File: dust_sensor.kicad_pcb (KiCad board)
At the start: 2 copper layers, 50 x 45 mm, 32 parts, among them P1 ADC, P10 PWR, P2 POWER, P3 LCD, P4 LCD_RST, P5 SERIAL, P6 DHT, P7 SENSOR, P8 GPIOS, P9 DEEP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

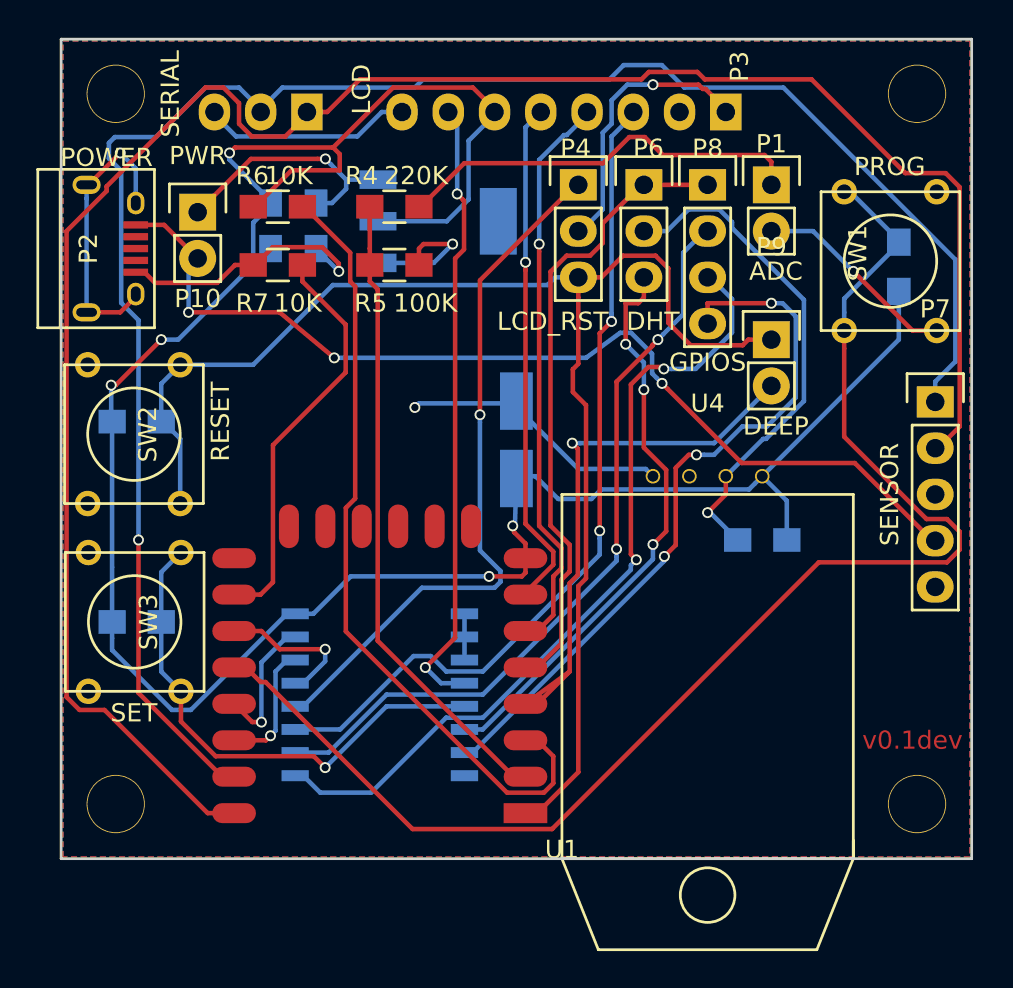
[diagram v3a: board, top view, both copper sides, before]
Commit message: PCB: remove LCD_RST jumper
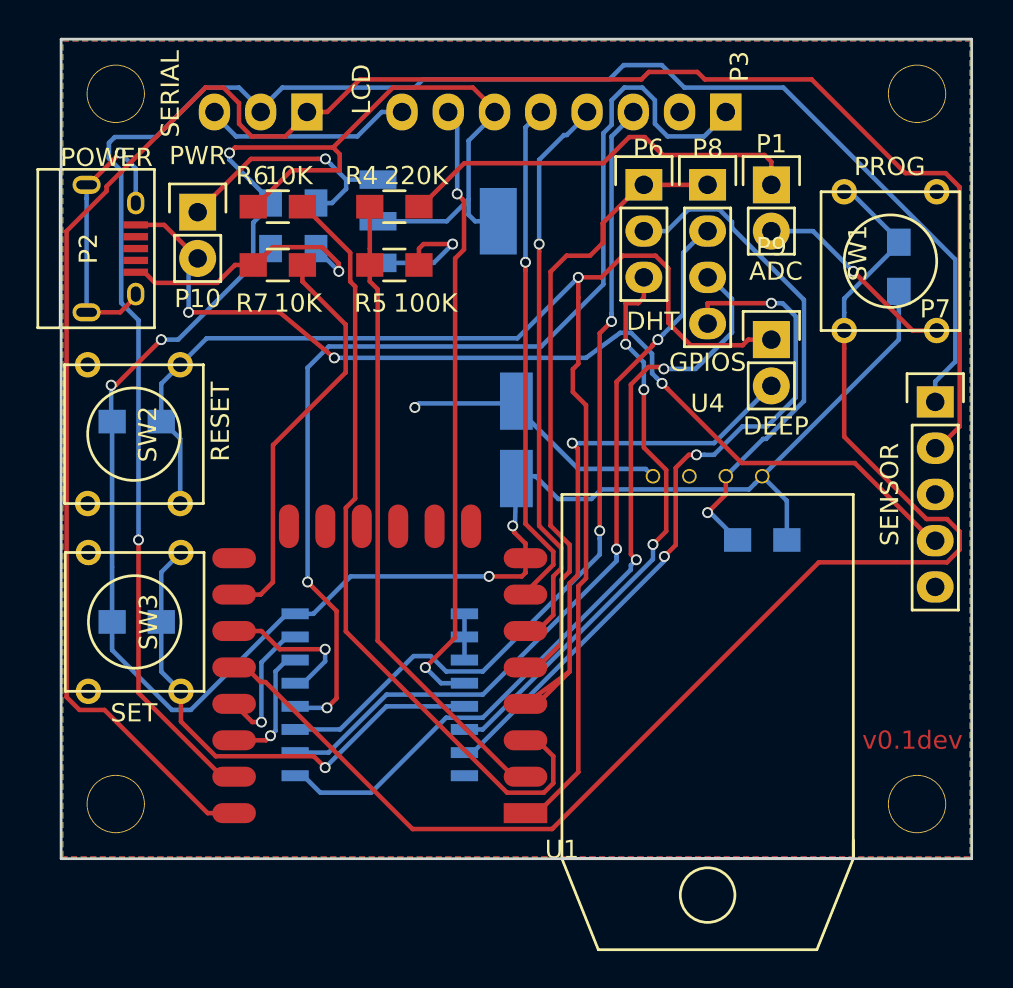
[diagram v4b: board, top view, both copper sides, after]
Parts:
- removed P4: LCD_RST, Pin_Headers:Pin_Header_Straight_1x03
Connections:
- P2 pad 2: Net-(P2-Pad2) -> (no net)
- P2 pad 3: Net-(P2-Pad3) -> (no net)
- P2 pad 4: Net-(P2-Pad4) -> (no net)
- P7 pad 5: Net-(P7-Pad5) -> (no net)
- U1 pad 10: Net-(U1-Pad10) -> (no net)
- U1 pad 11: Net-(U1-Pad11) -> (no net)
- U1 pad 12: Net-(U1-Pad12) -> (no net)
- U1 pad 13: Net-(U1-Pad13) -> (no net)
- U1 pad 14: Net-(U1-Pad14) -> (no net)
- U1 pad 9: Net-(U1-Pad9) -> (no net)
- U2 pad 4: (no net) -> +3V3
- U3 pad 12: Net-(P4-Pad1) -> Net-(P3-Pad1)
- U4 pad 3: Net-(U4-Pad3) -> (no net)
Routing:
- net Net-(P3-Pad1): track 15.5 -> 59.4 mm, vias 1 -> 2
- net Net-(P4-Pad1): track 38.7 -> 0.00 mm, vias 1 -> 0
- net +3V3: track 131.7 -> 134.4 mm
- net RESET: vias 0 -> 1

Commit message: PCB: SCH: choose ext_int/dht between GPIO2/GPIO14
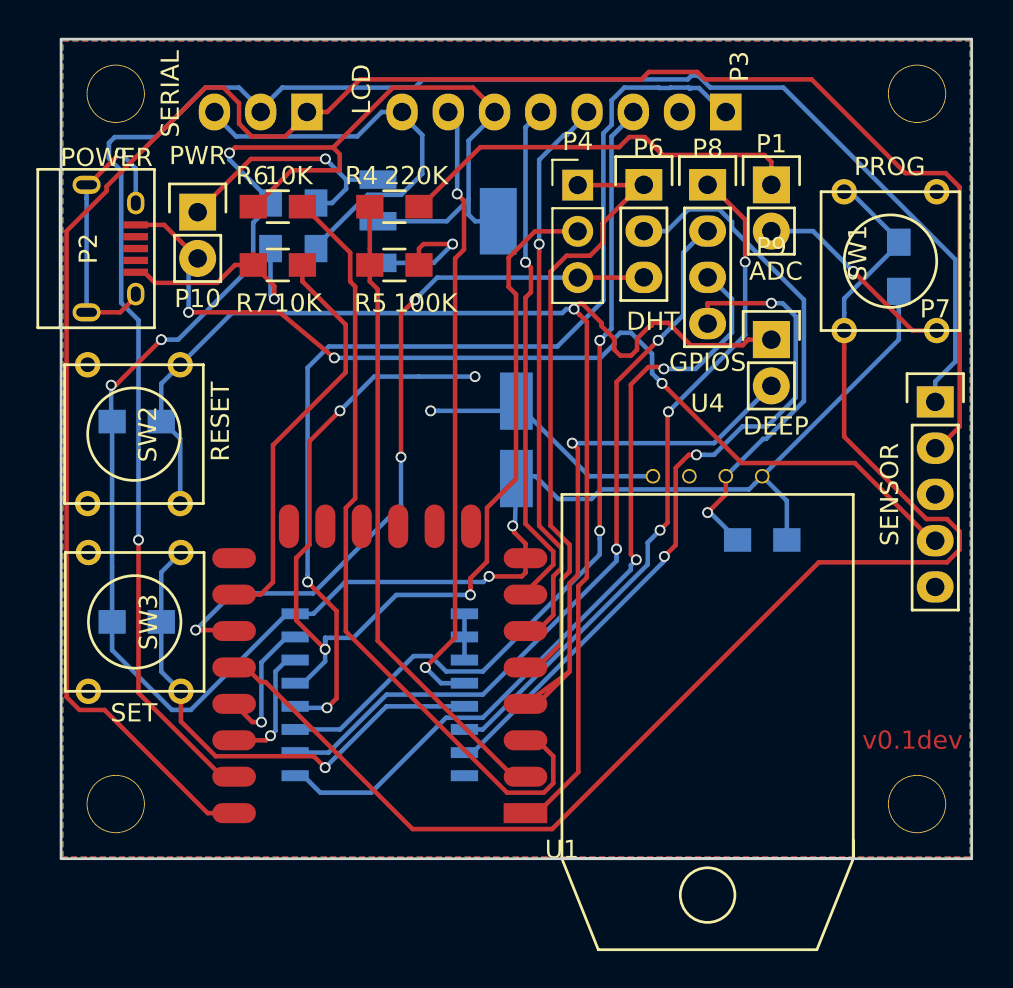
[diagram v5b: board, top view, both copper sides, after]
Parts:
- added P4: EXP_INT, Pin_Headers:Pin_Header_Straight_1x03_Pitch2.54mm, F.Cu at (67.9, 39.0)
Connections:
- P6 pad 1: DHT_GPIO -> GPIO14
- P6 pad 3: DHT_EXT -> GPIO2
- P8 pad 1: DHT_GPIO -> P2
- U1 pad 17: Net-(U1-Pad17) -> GPIO2
- U1 pad 5: DHT_GPIO -> GPIO14
- U3 pad 13: Net-(U1-Pad17) -> Net-(P4-Pad2)
- U3 pad 6: DHT_EXT -> P2
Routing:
- net Net-(P4-Pad2): track 0.00 -> 60.1 mm, vias 0 -> 4
- net GPIO2: track 0.00 -> 40.9 mm, vias 0 -> 3
- net P2: track 0.00 -> 37.8 mm, vias 0 -> 3
- net GPIO14: track 0.00 -> 34.9 mm
- net DHT_GPIO: track 34.8 -> 0.00 mm
- net DHT_EXT: track 31.7 -> 0.00 mm, vias 3 -> 0
- net Net-(U1-Pad17): track 8.88 -> 0.00 mm, vias 1 -> 0
- net GND: track 62.6 -> 71.1 mm
- net RESET: track 79.0 -> 75.6 mm
- net Net-(P3-Pad1): track 59.4 -> 58.3 mm

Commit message: SCH,PCB: Add GND/3.3V to GPIOS header, fix order of pins
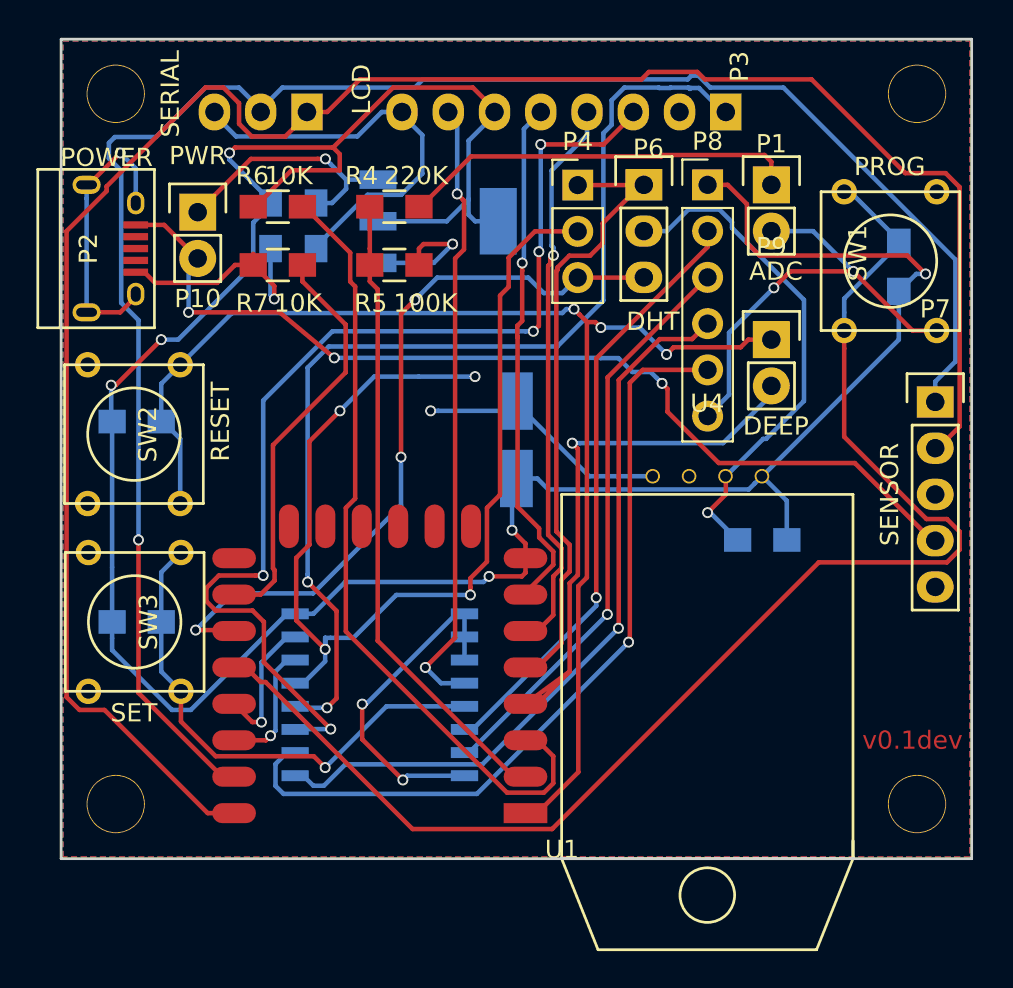
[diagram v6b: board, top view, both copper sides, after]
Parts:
- P8: footprint Pin_Headers:Pin_Header_Straight_1x04 -> Pin_Headers:Pin_Header_Straight_1x06_Pitch2.54mm
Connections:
- P8 pad 1: P2 -> +3V3
- P8 pad 2: P5 -> P2
- P8 pad 3: P4 -> P3
- P8 pad 4: P3 -> P4
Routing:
- net GND: track 71.1 -> 101.1 mm, vias 4 -> 7
- net +3V3: track 134.4 -> 151.1 mm, vias 5 -> 6
- net Net-(P3-Pad3): track 46.5 -> 59.6 mm, vias 2 -> 5
- net P3: track 39.6 -> 32.4 mm, vias 3 -> 1
- net P2: track 37.8 -> 33.3 mm, vias 3 -> 1
- net P4: track 44.8 -> 41.4 mm, vias 2 -> 1
- net RESET: track 75.6 -> 72.4 mm, vias 1 -> 3
- net P5: track 42.3 -> 44.4 mm, vias 2 -> 1
- net +5V: track 56.1 -> 54.9 mm
- net Net-(P1-Pad1): track 22.8 -> 21.9 mm
- net GPIO2: track 40.9 -> 41.6 mm

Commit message: PCB: change version to v0.4dev
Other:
- board text added: "v0.4dev"
- board text removed: "v0.1dev"
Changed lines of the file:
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@@
     (links 82)
     (no_connects 0)
-    (area 39.424999 30.924999 89.575001 76.075001)
+    (area 37.762459 24.124999 89.575001 82.176201)
     (thickness 1.6)
     (drawings 5)
@@
     )
   )
-  (gr_text v0.1dev (at 86.25 69.5) (layer F.Cu)
+  (gr_text v0.4dev (at 86.25 69.5) (layer F.Cu)
     (effects (font (size 1 1) (thickness 0.2)))
   )

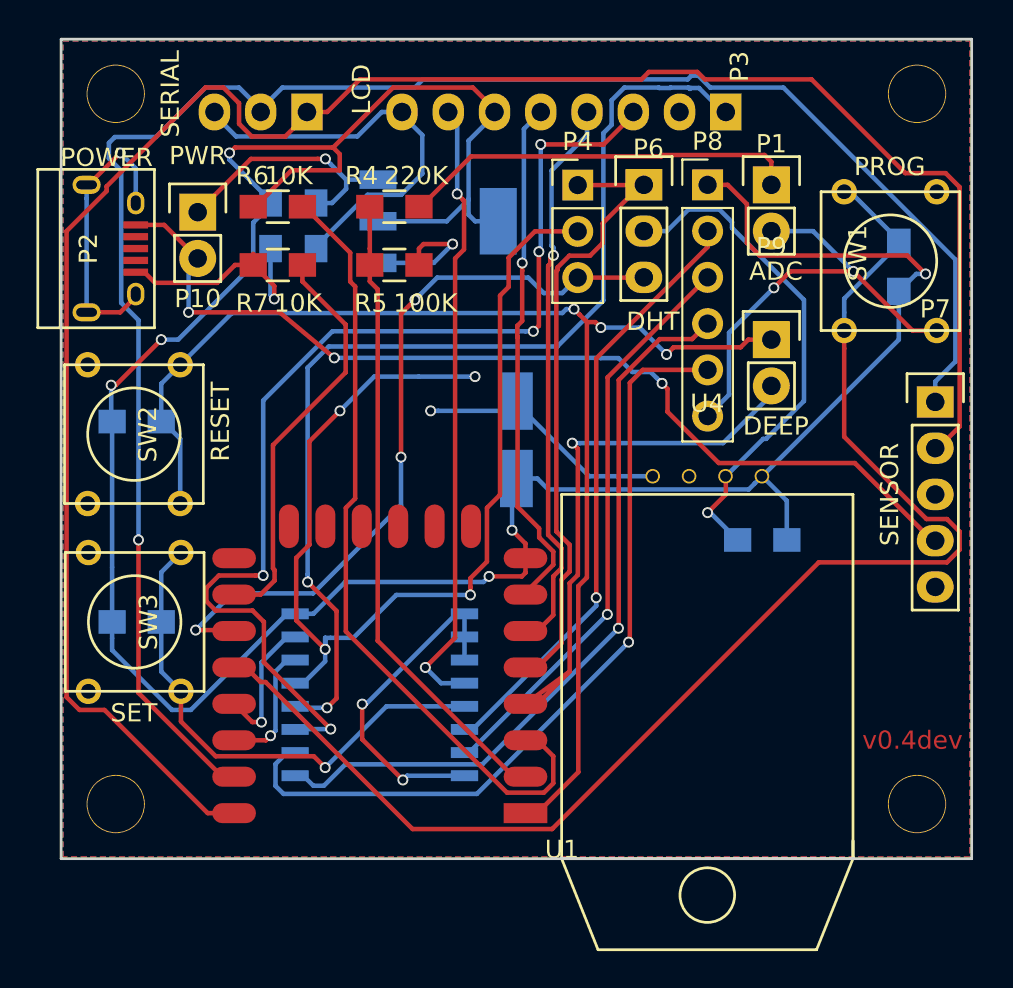
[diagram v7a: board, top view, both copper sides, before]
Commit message: PCB: SCH: Add header for BMP180/280
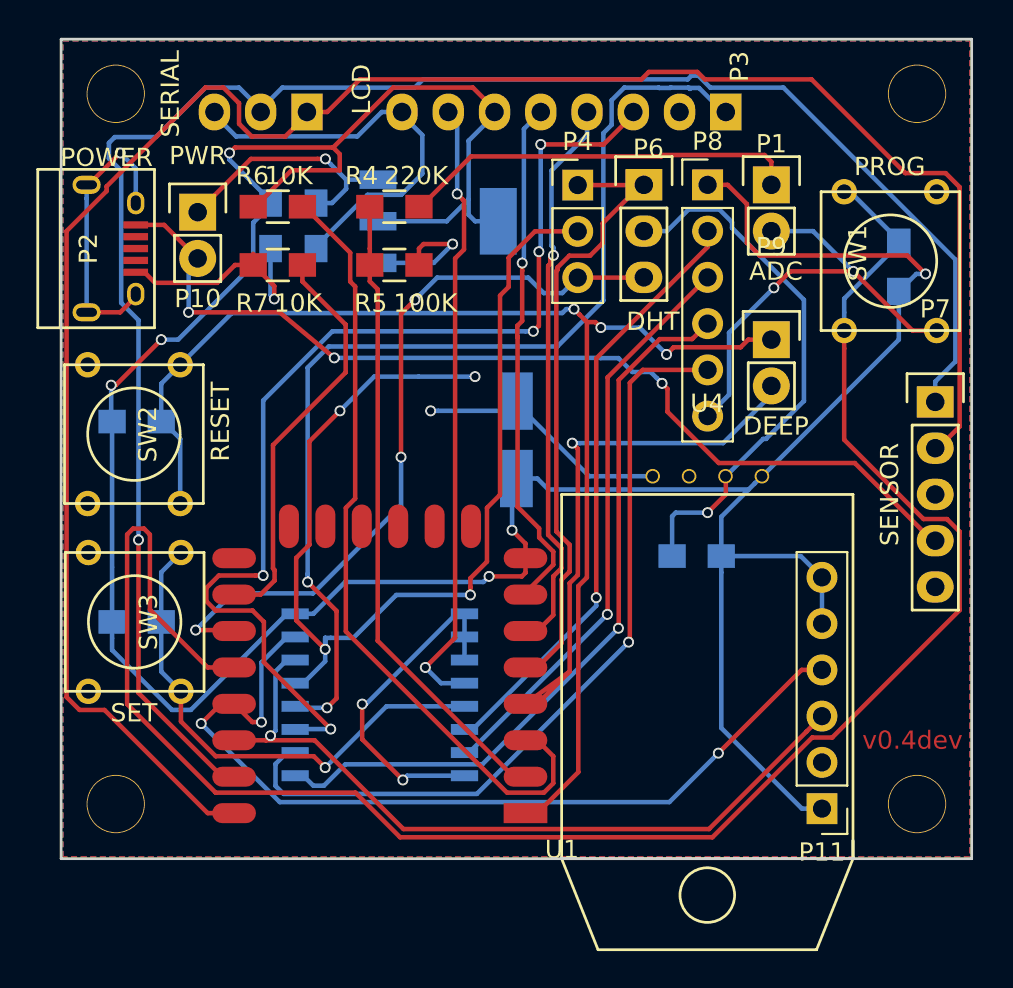
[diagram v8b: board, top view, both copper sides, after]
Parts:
- added P11: BMPx80, Pin_Headers:Pin_Header_Straight_1x06_Pitch2.54mm, F.Cu at (81.3, 73.3)
- moved R8 3.71 mm to (74.4, 59.4)
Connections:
- net Net-(U1-Pad19) renamed SDA
- net Net-(U1-Pad20) renamed SCL
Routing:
- net SDA: track 7.62 -> 48.8 mm, vias 1 -> 3
- net SCL: track 7.08 -> 42.2 mm
- net PROG: track 75.5 -> 104.5 mm
- net +3V3: track 151.1 -> 176.7 mm
- net Net-(P6-Pad2): track 27.8 -> 29.9 mm
